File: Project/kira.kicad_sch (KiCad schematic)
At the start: 35 parts, among them J1 USB_C_Receptacle_USB2.0, J2 SWD, J3 Conn_01x04_Male, SW46 Boot, SW47 Reset, U1 RP2040, U2 XC6206PxxxMR, U3 W25Q128JVS, U4 USBLC6-2SC6, Y1 12MHz

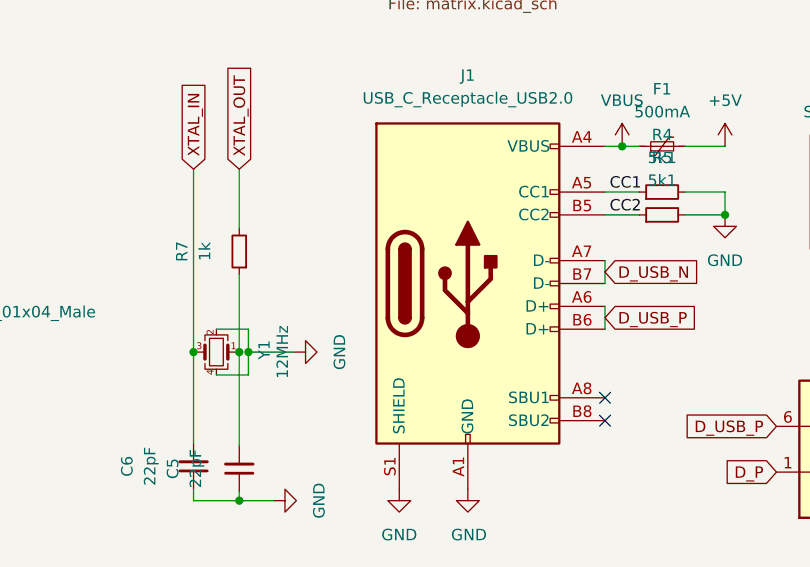
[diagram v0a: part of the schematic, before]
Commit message: changed footprints to ebastler
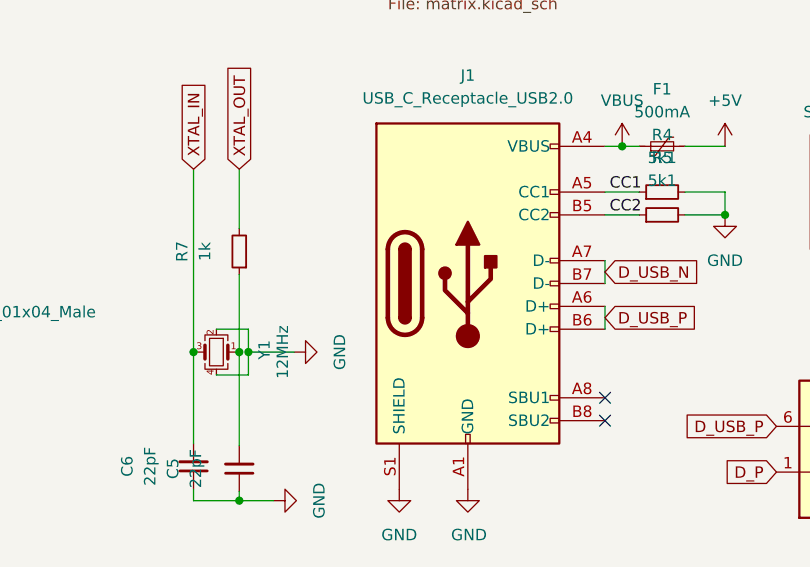
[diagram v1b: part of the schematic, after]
